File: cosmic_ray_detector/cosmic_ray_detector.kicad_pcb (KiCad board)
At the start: 4 copper layers, 80 x 60 mm, 57 parts, among them J1 MOLEX micro-fit 43045-0210, J2 5 pin pin header, J3 Black Banana, J4 Red Banana, J5 Green Banana, J6 BNC, U1 TL072, U2 TPS7A30, U3 TPS7A49, U4 TLV3501AIDBVTG4, U5 AD5270BRMZ-100-RL7

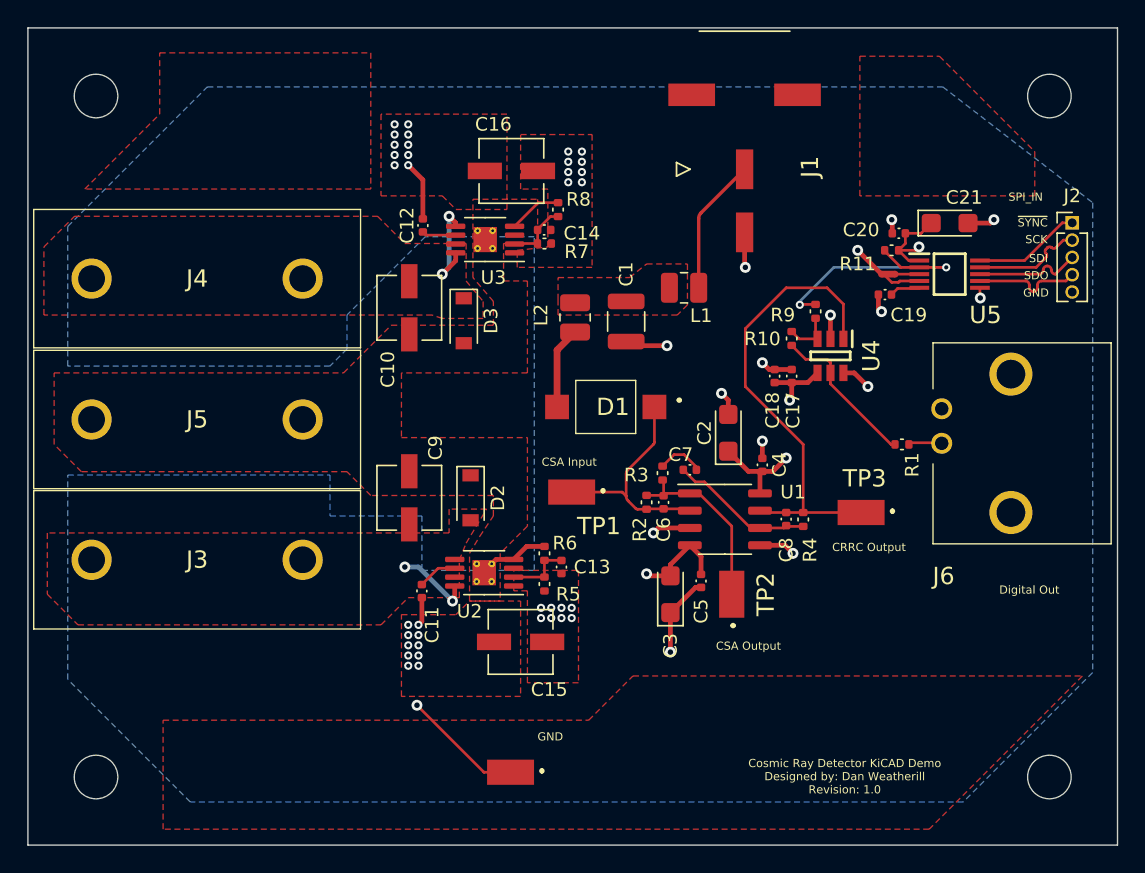
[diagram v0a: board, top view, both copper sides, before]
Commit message: update routed / finished PCB to version 9
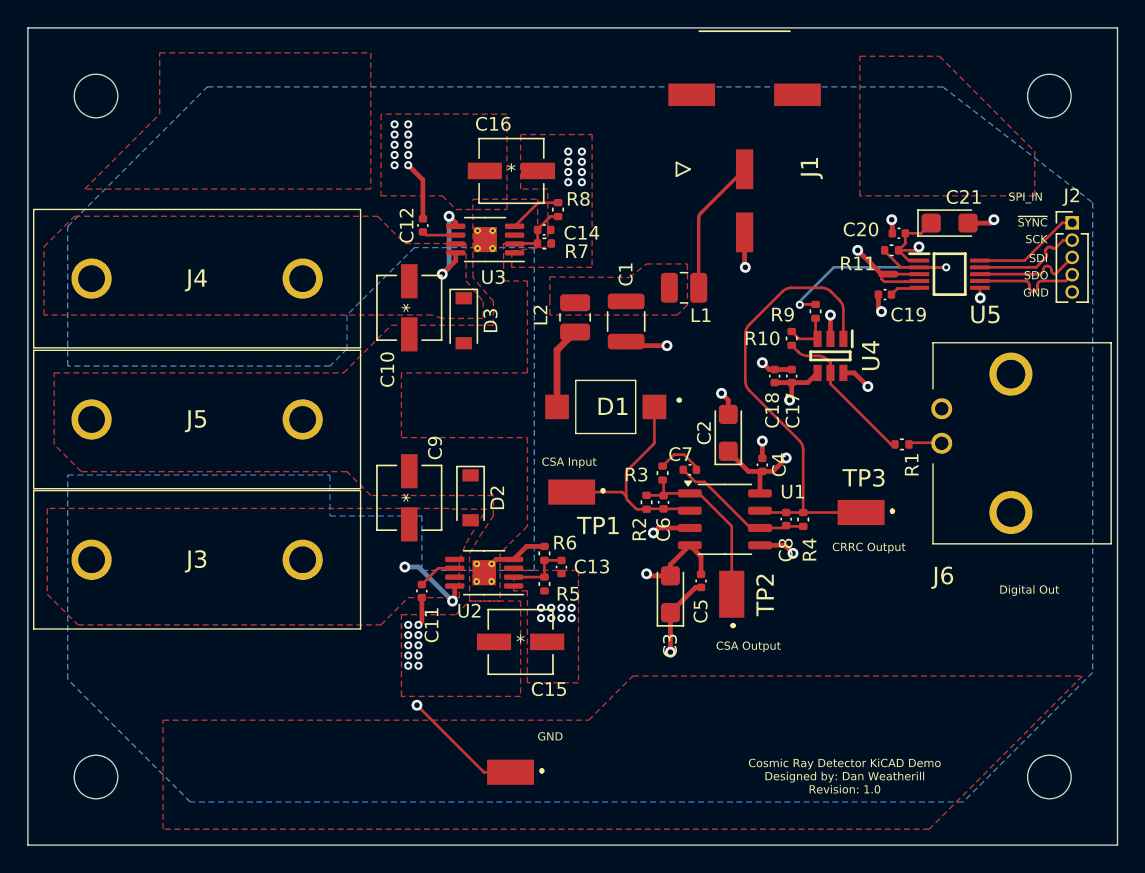
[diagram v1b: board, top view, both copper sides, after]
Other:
- rule pad_to_mask_clearance: 0.125 -> 0.1

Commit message: update pcb and schem to V10
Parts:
- C11, C12, C13, C14, C17, C18, C19, C20, C4, C5, C6, C7, C8: footprint cosmic_ray_detector_lib:C_0402_1005Metric -> Capacitor_SMD:C_0402_1005Metric
- D2, D3: footprint cosmic_ray_detector_lib:D_SOD-123 -> Diode_SMD:D_SOD-123
- R1, R10, R11, R2, R3, R4, R5, R6, R7, R8, R9: footprint cosmic_ray_detector_lib:R_0402_1005Metric -> Resistor_SMD:R_0402_1005Metric
- TP4: value ~ -> TestPoint
- renumbered REF** to H1, REF** to H2, REF** to H3, REF** to H4
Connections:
- J2 pad 1: /threshold_setting/SPI.~{SYNC} -> /SPI.~{SYNC}
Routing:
- net GNDA: track 61.2 -> 61.8 mm
- added copper zone on In1.Cu, net GNDA
- added copper zone on In2.Cu, net GNDA
- removed copper zone on F.Cu, net (none)
- removed copper zone on In1.Cu, net (none)
- removed copper zone on In2.Cu, net (none)
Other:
- outline, holes or cut-outs redrawn
- board text added: "Cosmic Ray Detector KiCAD Demo Designed by: Dan Weatherill Revision: ${PROJ_REV}"
- board text removed: "Cosmic Ray Detector KiCAD Demo Designed by: Dan Weatherill Revision: 1.0"

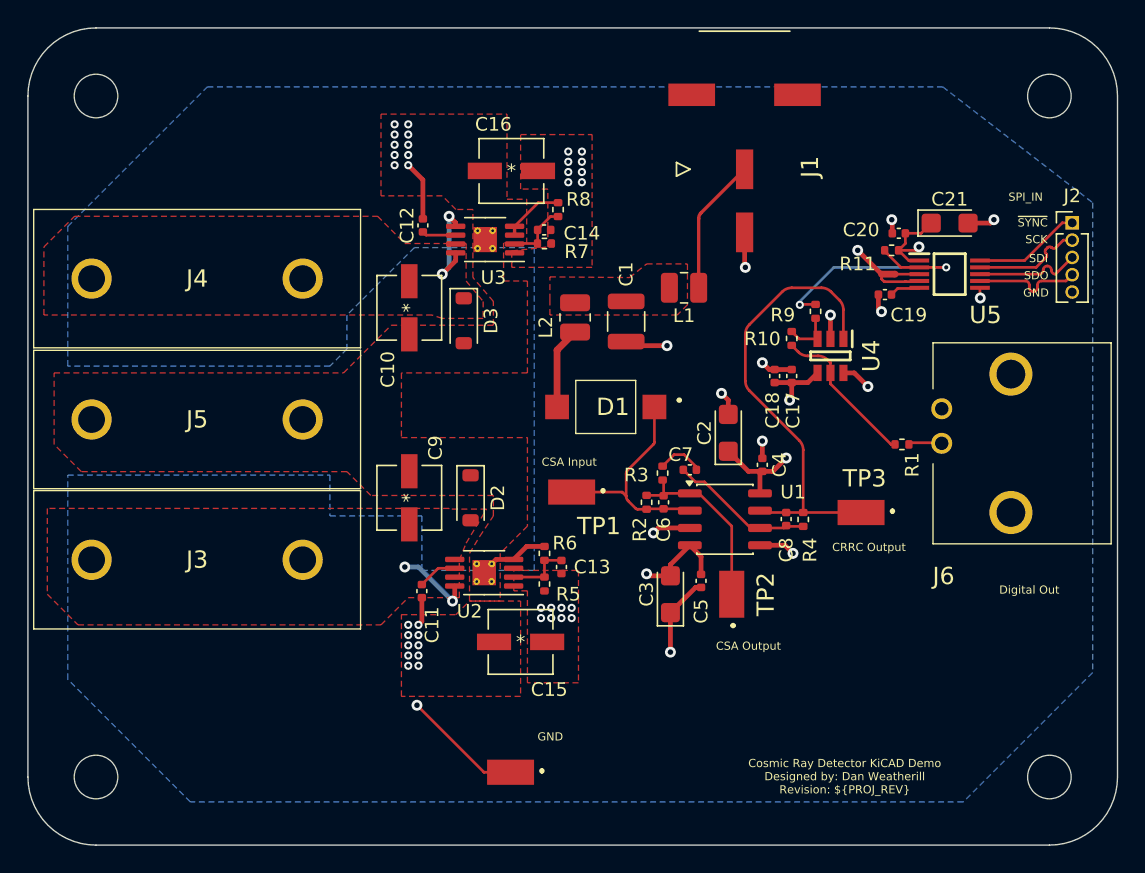
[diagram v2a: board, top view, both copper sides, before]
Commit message: update blank PCB to V10
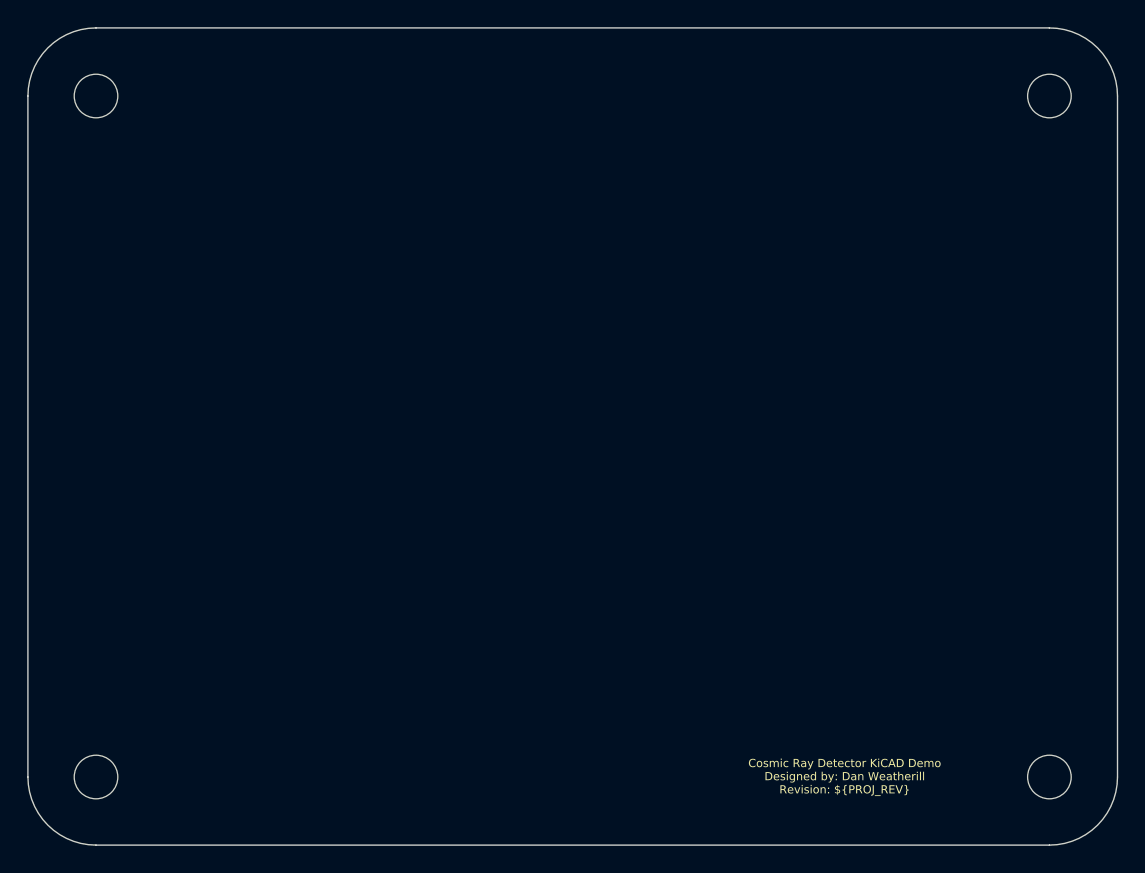
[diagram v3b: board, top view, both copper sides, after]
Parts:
- removed C1: C, Capacitor_SMD:C_1210_3225Metric
- removed C10, C15, C16, C9: 10uF, cosmic_ray_detector_lib:MAL215375109E3
- removed C11, C12: 22nF, Capacitor_SMD:C_0402_1005Metric
- removed C13, C14: 10nF, Capacitor_SMD:C_0402_1005Metric
- removed C17, C20, C4, C5: 0.1uF, Capacitor_SMD:C_0402_1005Metric
- removed C18: 2.2uF, Capacitor_SMD:C_0402_1005Metric
- removed C19: 1uF, Capacitor_SMD:C_0402_1005Metric
- removed C2, C21, C3: 10uF, Capacitor_Tantalum_SMD:CP_EIA-3216-12_Kemet-S
- removed C6: C, Capacitor_SMD:C_0402_1005Metric
- removed C7, C8: ~, Capacitor_SMD:C_0402_1005Metric
- removed D1: VBPW34FAS, cosmic_ray_detector_lib:VBPW34FAS
- removed D2, D3: 12V, Diode_SMD:D_SOD-123
- removed J1: MOLEX micro-fit 43045-0210, cosmic_ray_detector_lib:4304502_09
- removed J2: 5 pin pin header, Connector_PinHeader_1.27mm:PinHeader_1x05_P1.27mm_Vertical
- removed J3: Black Banana, cosmic_ray_detector_lib:242432
- removed J4: Red Banana, cosmic_ray_detector_lib:242431
- removed J5: Green Banana, cosmic_ray_detector_lib:242434
- removed J6: BNC, cosmic_ray_detector_lib:MOLEX_731375003
- removed L1, L2: L, Inductor_SMD:L_1008_2520Metric
- removed NT1: NetTie_2, NetTie:NetTie-2_SMD_Pad0.5mm
- removed R1, R10, R11, R2: R_US, Resistor_SMD:R_0402_1005Metric
- removed R3, R4, R9: ~, Resistor_SMD:R_0402_1005Metric
- removed R5: 13k, Resistor_SMD:R_0402_1005Metric
- removed R6, R8: 10k, Resistor_SMD:R_0402_1005Metric
- removed R7: 12.7k, Resistor_SMD:R_0402_1005Metric
- removed TP1, TP4: TestPoint, cosmic_ray_detector_lib:harwin_tp_SMD
- removed TP2, TP3: ~, cosmic_ray_detector_lib:harwin_tp_SMD
- removed U1: TL072, Package_SO:SO-8_3.9x4.9mm_P1.27mm
- removed U2: TPS7A30, cosmic_ray_detector_lib:MSOP-8-1EP_3x3mm_P0.65mm_EP1.73x1.85mm_ThermalVias
- removed U3: TPS7A49, cosmic_ray_detector_lib:MSOP-8-1EP_3x3mm_P0.65mm_EP1.73x1.85mm_ThermalVias
- removed U4: TLV3501AIDBVTG4, cosmic_ray_detector_lib:SOT95P280X145-6N
- removed U5: AD5270BRMZ-100-RL7, cosmic_ray_detector_lib:SOP50P490X110-10N
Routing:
- net GNDA: track 61.8 -> 0.00 mm, vias 36 -> 0
- net /comparator/V_IN: track 33.9 -> 0.00 mm
- net +5VA: track 18.9 -> 0.00 mm, vias 11 -> 0
- net /comparator/VREF: track 18.3 -> 0.00 mm, vias 2 -> 0
- net /detector_frontend/CSA_IN: track 16.7 -> 0.00 mm
- net /detector_frontend/CSA_FB: track 12.6 -> 0.00 mm
- net /comparator/COMP_OUT: track 11.4 -> 0.00 mm
- net Net-(U1B--): track 10.7 -> 0.00 mm
- net /BIAS_IN: track 10.1 -> 0.00 mm
- net /threshold_setting/SPI.SCK: track 8.06 -> 0.00 mm
- net /threshold_setting/SPI.SDO: track 7.95 -> 0.00 mm
- net /threshold_setting/SPI.~{SYNC}: track 7.92 -> 0.00 mm
- net /threshold_setting/SPI.SDI: track 7.92 -> 0.00 mm
- net /Power Regulators/+VIN: track 7.36 -> 0.00 mm, vias 2 -> 0
- net -5VA: track 7.12 -> 0.00 mm, vias 9 -> 0
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- removed copper zone on F.Cu, net +5VA
- removed copper zone on In1.Cu, net +5VA
- removed copper zone on F.Cu, net -5VA
- removed copper zone on In2.Cu, net -5VA
- removed copper zone on F.Cu, net /Power Regulators/+VIN
- removed copper zone on F.Cu, net /Power Regulators/-VIN
- removed copper zone on F.Cu, net /T_MID
- removed copper zone on B.Cu, net GNDA
- removed copper zone on F.Cu, net GNDA
- removed copper zone on In1.Cu, net GNDA
- removed copper zone on In2.Cu, net GNDA
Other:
- board text removed: "CRRC Output"
- board text removed: "CSA Input"
- board text removed: "CSA Output"
- board text removed: "Digital Out"
- board text removed: "GND"
- board text removed: "NOTE: Always follow datasheet recommendations on layout, especially for regulators & the like. Here, note that the pin {dblquote}5{dblquote} is just the {dblquote}enable{dblquote} pin, we really want all the current through VIN net to go to pin 8"
- board text removed: "SCK"
- board text removed: "SDI"
- board text removed: "SDO"
- board text removed: "SPI_IN"
- board text removed: "~{SYNC}"
